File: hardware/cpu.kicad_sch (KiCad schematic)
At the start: 16 parts, among them J1 Conn_02x02_Odd_Even, U3 ESP32-C3-WROOM-02

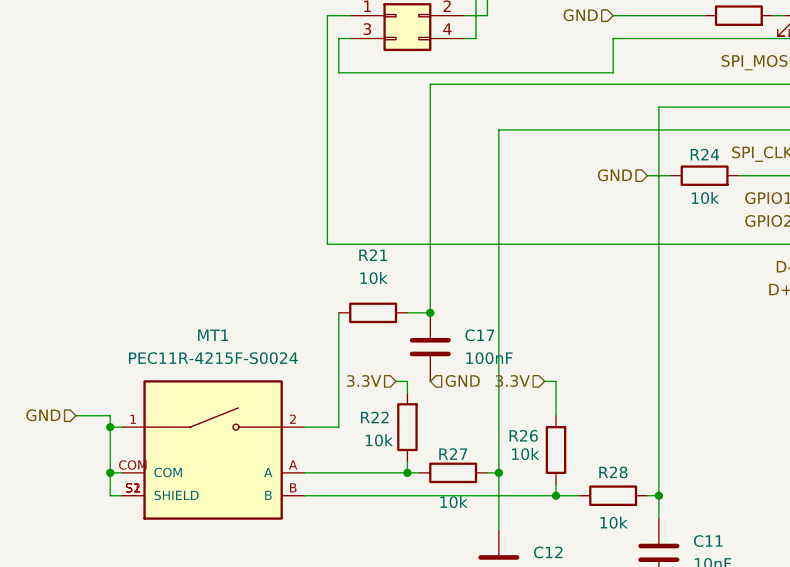
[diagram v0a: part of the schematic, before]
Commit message: Remove useless 10k resistor for PEC11 switch.
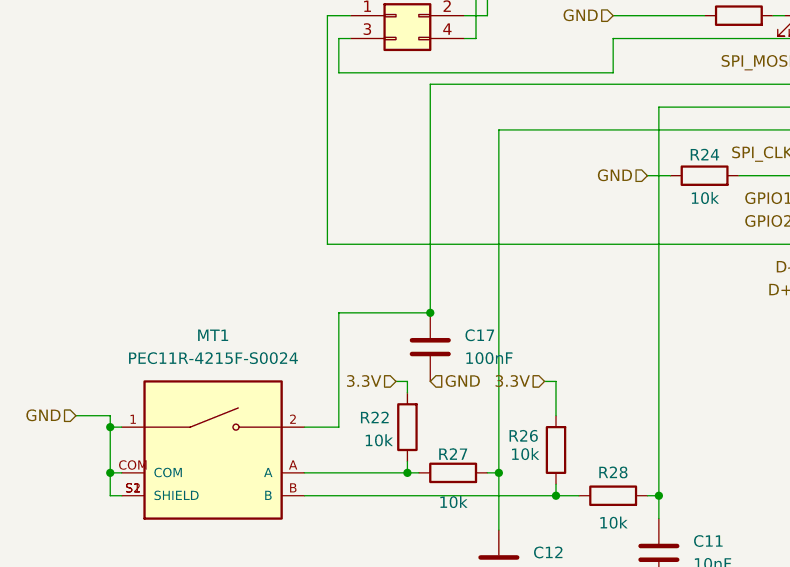
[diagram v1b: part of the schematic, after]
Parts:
- removed R21: 10k, Resistor_SMD:R_0805_2012Metric, symbol Device:R
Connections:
- net at MT1.2: now also C17.1, U3.15 (IO3)
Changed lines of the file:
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@@
+	(wire
+		(pts
+			(xy 62.23 93.98) (xy 72.39 93.98)
+		)
+		(stroke
+			(width 0)
+			(type default)
+		)
+	)
 	(wire
 		(pts
@@
 		(pts
 			(xy 78.74 27.94) (xy 78.74 60.96)
-		)
-		(stroke
-			(width 0)
-			(type default)
-		)
-	)
-	(wire
-		(pts
-			(xy 69.85 93.98) (xy 72.39 93.98)
 		)
 		(stroke
@@
 					(unit 1)
 				)
-			)
-		)
-	)
-	(symbol
-		(lib_id "Device:R")
-		(at 66.04 93.98 90)
-		(unit 1)
-		(exclude_from_sim no)
-		(in_bom yes)
-		(on_board yes)
-		(dnp no)
-		(fields_autoplaced yes)
-		(property "Reference" "R21"
-			(at 66.04 87.63 90)
-			(effects
-				(font
-					(size 1.27 1.27)
-				)
-			)
-		)
-		(property "Value" "10k"
-			(at 66.04 90.17 90)
-			(effects
-				(font
-					(size 1.27 1.27)
-				)
-			)
-		)
-		(property "Footprint" "Resistor_SMD:R_0805_2012Metric"
-			(at 66.04 95.758 90)
-			(effects
-				(font
-					(size 1.27 1.27)
-				)
-				(hide yes)
-			)
-		)
-		(property "Datasheet" "~"
-			(at 66.04 93.98 0)
-			(effects
-				(font
-					(size 1.27 1.27)
-				)
-				(hide yes)
-			)
-		)
-		(property "Description" "Resistor"
-			(at 66.04 93.98 0)
-			(effects
-				(font
-					(size 1.27 1.27)
-				)
-				(hide yes)
-			)
-		)
-		(pin "1"
-		)
-		(pin "2"
-		)
-		(instances
-			(project "nixie_clock"
-				(path "/90430e5f-7049-4de8-b92d-f897c4a89819/99bf9233-4f4b-4c20-a5a1-eeea9a6ff67a"
-					(reference "R21")
-					(unit 1)
-				)

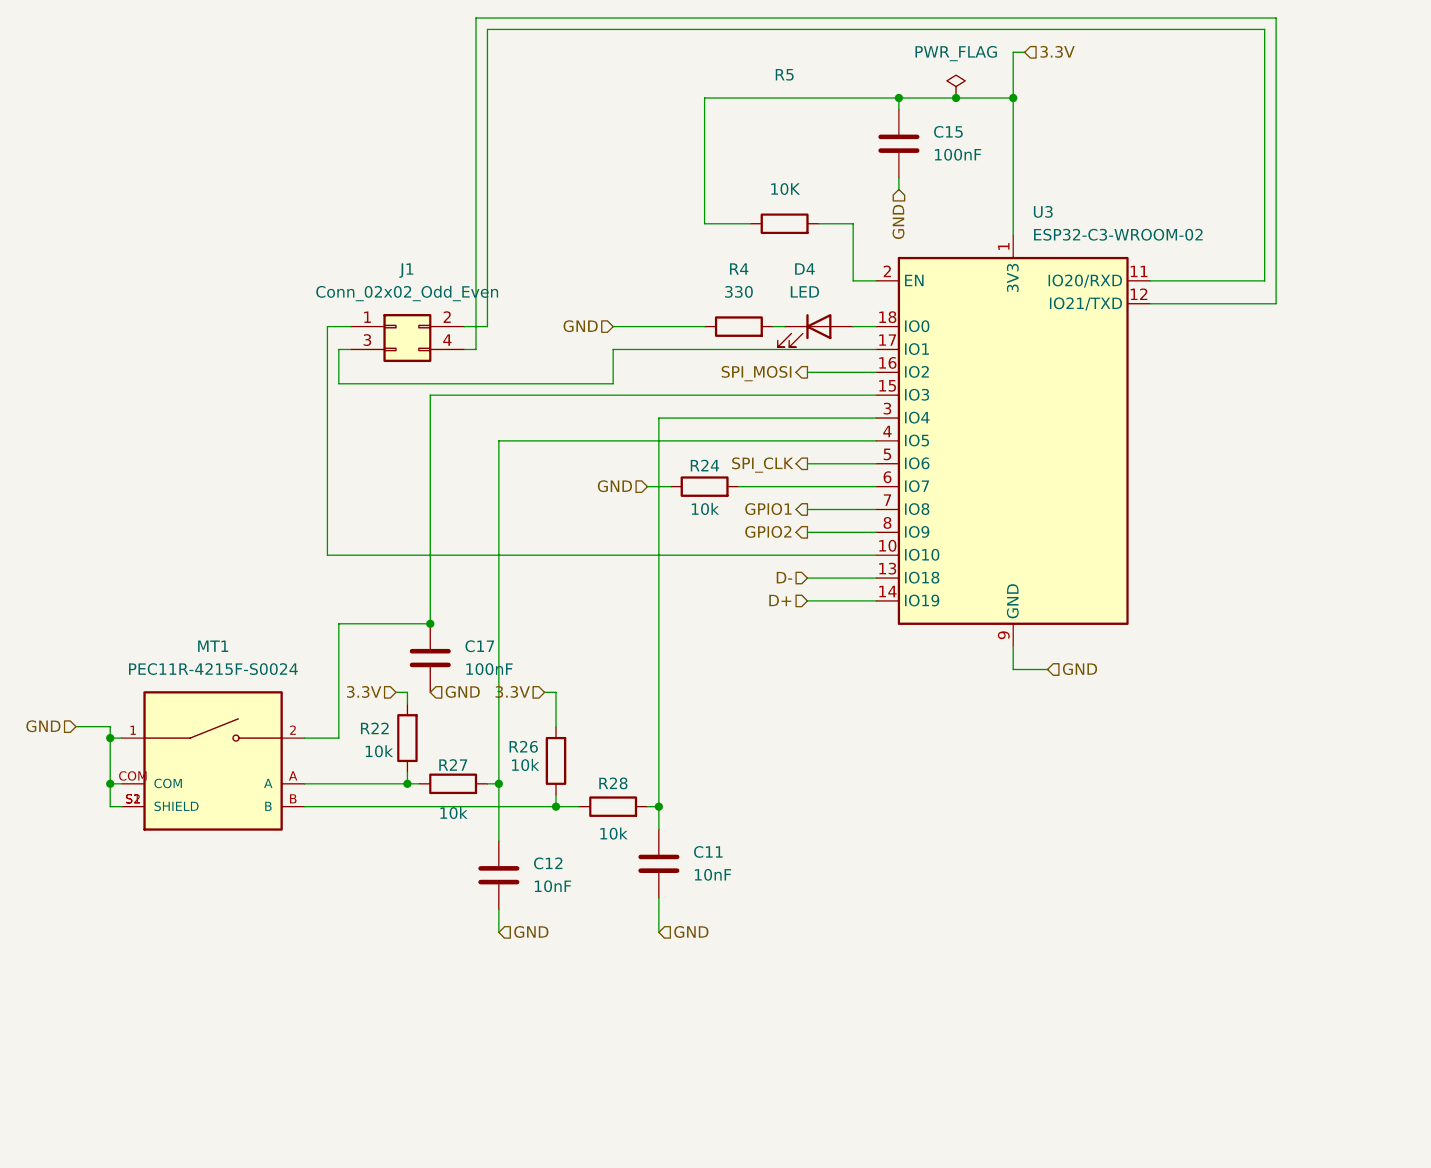
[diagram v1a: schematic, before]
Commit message: Add BOOT1 and RESET1 buttons. Add pullups on Boot strapping pins GPIO8,9. Fix EN, enable input.
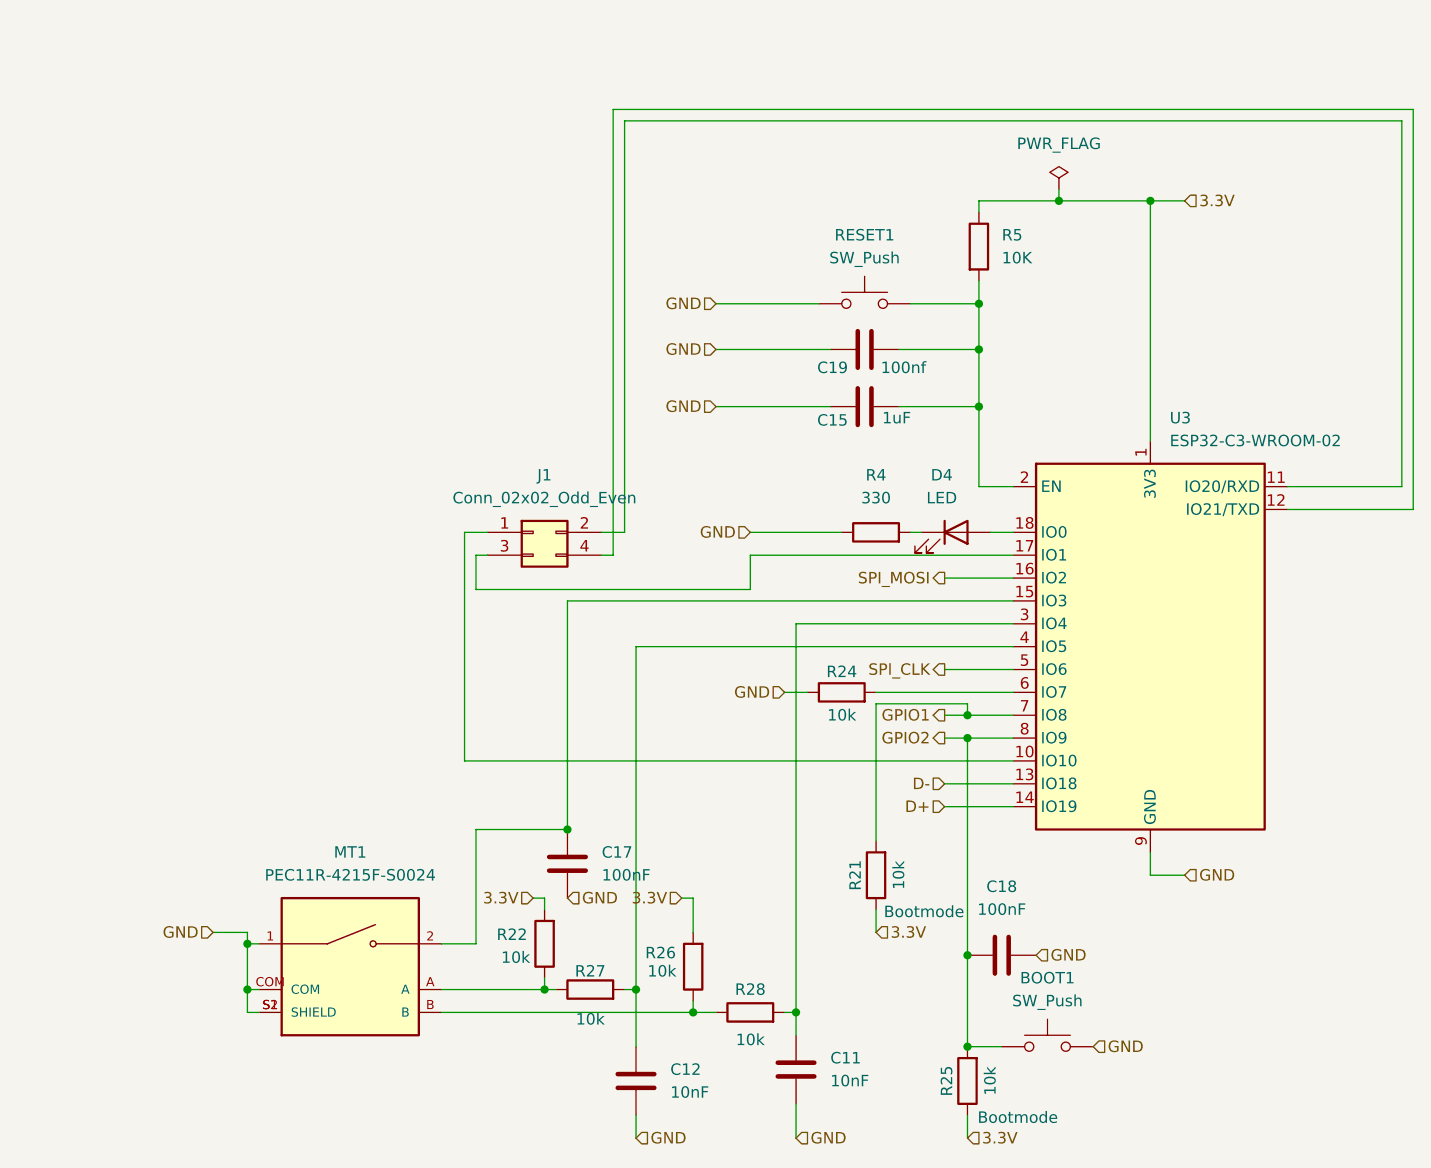
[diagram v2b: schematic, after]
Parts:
- added BOOT1, RESET1: SW_Push, Button_Switch_SMD:SW_SPST_Omron_B3FS-100xP, symbol Switch:SW_Push
- added C18: 100nF, Resistor_SMD:R_0805_2012Metric, symbol Device:C
- added C19: 100nf, Resistor_SMD:R_0805_2012Metric, symbol Device:C
- added R21, R25: 10k, Resistor_SMD:R_0805_2012Metric, symbol Device:R
- C15: value 100nF -> 1uF
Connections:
- net 3.3V: now also R21.1, R25.1; no longer C15.1
- net GND: now also C15.1, BOOT1.2, C18.2, C19.1, RESET1.1; no longer C15.2
- net GPIO1: now also R21.2
- net GPIO2: now also BOOT1.1, C18.1, R25.2
- net at R5.2, U3.2 (EN): now also C15.2, C19.2, RESET1.2
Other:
- moved on the sheet: C11, C12, C15, C17, D4, J1, MT1, R22, R24, R26, R27, R28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

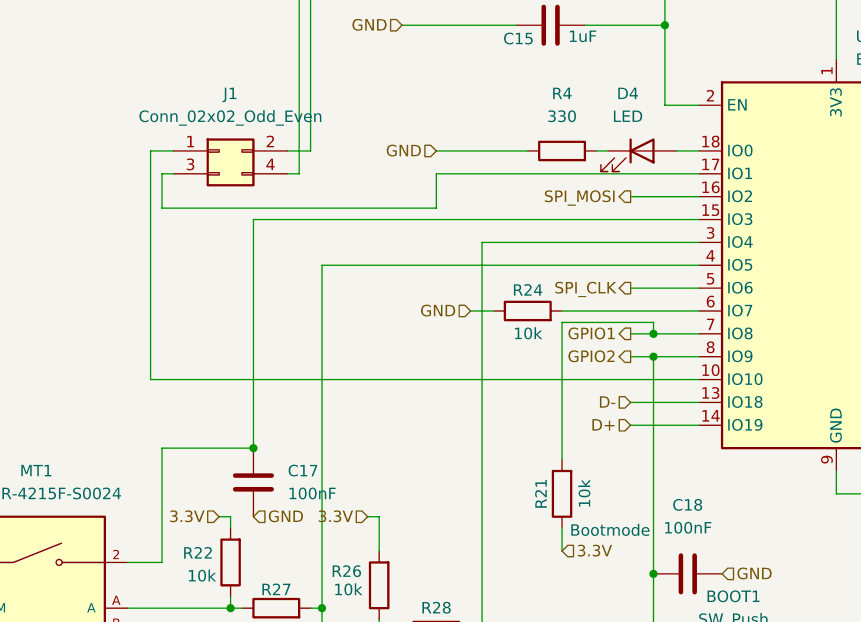
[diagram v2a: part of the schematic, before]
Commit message: Remap /LE and /BL to GPIO2 and GPIO1. SPI2 clk to GPIO6, SPI2 data to GPIO7.
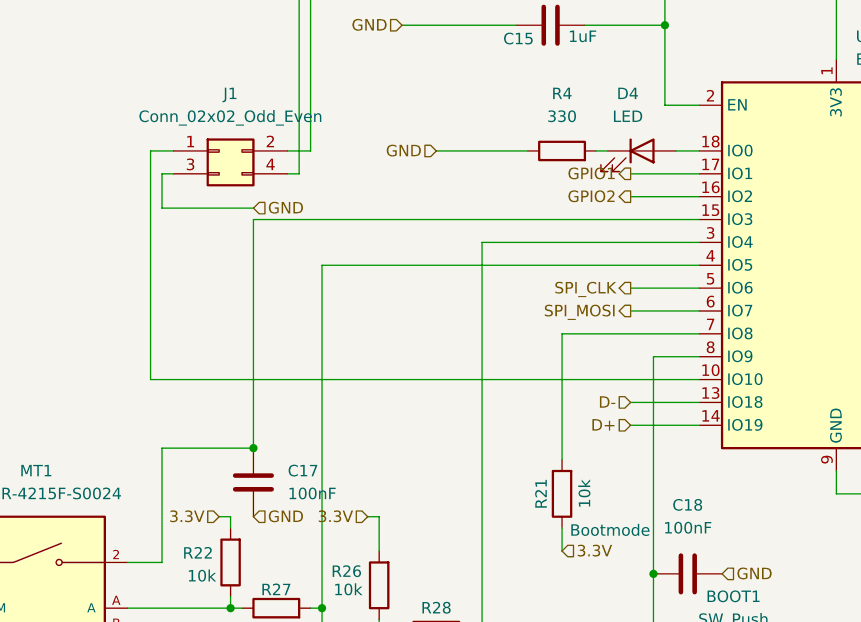
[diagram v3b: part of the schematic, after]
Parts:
- removed R24: 10k, Resistor_SMD:R_0805_2012Metric, symbol Device:R
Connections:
- net GND: now also J1.3 (Pin_3)
- net GPIO1: now also U3.17 (IO1); no longer R21.2, U3.7 (IO8)
- net GPIO2: now also U3.16 (IO2); no longer BOOT1.1, C18.1, R25.2, U3.8 (IO9)
- net SPI_MOSI: now also U3.6 (IO7); no longer U3.16 (IO2)
- new net: BOOT1.1, C18.1, R25.2, U3.8 (IO9)
- new net: R21.2, U3.7 (IO8)
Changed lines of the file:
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@@
-	)
-	(junction
-		(at 132.08 106.68)
-		(diameter 0)
-		(color 0 0 0 0)
 	)
 	(junction
@@
 	)
 	(junction
-		(at 132.08 104.14)
-		(diameter 0)
-		(color 0 0 0 0)
-	)
-	(junction
 		(at 133.35 58.42)
 		(diameter 0)
@@
 	(wire
 		(pts
-			(xy 129.54 104.14) (xy 132.08 104.14)
-		)
-		(stroke
-			(width 0)
-			(type default)
-		)
-	)
-	(wire
-		(pts
 			(xy 77.47 129.54) (xy 77.47 116.84)
 		)
@@
 	(wire
 		(pts
-			(xy 111.76 101.6) (xy 114.3 101.6)
-		)
-		(stroke
-			(width 0)
-			(type default)
-		)
-	)
-	(wire
-		(pts
 			(xy 132.08 106.68) (xy 132.08 130.81)
 		)
@@
 	(wire
 		(pts
-			(xy 132.08 102.87) (xy 121.92 102.87)
+			(xy 121.92 104.14) (xy 137.16 104.14)
 		)
 		(stroke
@@
 	(wire
 		(pts
-			(xy 132.08 104.14) (xy 132.08 102.87)
-		)
-		(stroke
-			(width 0)
-			(type default)
-		)
-	)
-	(wire
-		(pts
 			(xy 76.2 109.22) (xy 76.2 83.82)
 		)
@@
 	(wire
 		(pts
-			(xy 107.95 90.17) (xy 77.47 90.17)
+			(xy 129.54 86.36) (xy 137.16 86.36)
 		)
 		(stroke
@@
 	(wire
 		(pts
+			(xy 129.54 88.9) (xy 137.16 88.9)
+		)
+		(stroke
+			(width 0)
+			(type default)
+		)
+	)
+	(wire
+		(pts
 			(xy 104.14 63.5) (xy 116.84 63.5)
 		)
@@
 	(wire
 		(pts
-			(xy 107.95 86.36) (xy 107.95 90.17)
-		)
-		(stroke
-			(width 0)
-			(type default)
-		)
-	)
-	(wire
-		(pts
-			(xy 129.54 88.9) (xy 137.16 88.9)
-		)
-		(stroke
-			(width 0)
-			(type default)
-		)
-	)
-	(wire
-		(pts
 			(xy 113.03 137.16) (xy 111.76 137.16)
 		)
@@
 	(wire
 		(pts
-			(xy 121.92 102.87) (xy 121.92 118.11)
+			(xy 121.92 104.14) (xy 121.92 118.11)
 		)
 		(stroke
@@
 	(wire
 		(pts
+			(xy 129.54 101.6) (xy 137.16 101.6)
+		)
+		(stroke
+			(width 0)
+			(type default)
+		)
+	)
+	(wire
+		(pts
 			(xy 92.71 36.83) (xy 181.61 36.83)
 		)
@@
 	(wire
 		(pts
+			(xy 77.47 90.17) (xy 87.63 90.17)
+		)
+		(stroke
+			(width 0)
+			(type default)
+		)
+	)
+	(wire
+		(pts
 			(xy 133.35 78.74) (xy 137.16 78.74)
 		)
@@
 	(wire
 		(pts
-			(xy 132.08 104.14) (xy 137.16 104.14)
-		)
-		(stroke
-			(width 0)
-			(type default)
-		)
-	)
-	(wire
-		(pts
 			(xy 133.35 63.5) (xy 133.35 69.85)
 		)
@@
 	(wire
 		(pts
-			(xy 129.54 106.68) (xy 132.08 106.68)
-		)
-		(stroke
-			(width 0)
-			(type default)
-		)
-	)
-	(wire
-		(pts
 			(xy 95.25 134.62) (xy 95.25 140.97)
 		)
@@
 	(wire
 		(pts
-			(xy 107.95 86.36) (xy 137.16 86.36)
-		)
-		(stroke
-			(width 0)
-			(type default)
-		)
-	)
-	(wire
-		(pts
 			(xy 133.35 69.85) (xy 133.35 78.74)
 		)
@@
 	(wire
 		(pts
-			(xy 121.92 101.6) (xy 137.16 101.6)
-		)
-		(stroke
-			(width 0)
-			(type default)
-		)
-	)
-	(wire
-		(pts
 			(xy 83.82 124.46) (xy 85.09 124.46)
 		)
@@
 			(width 0)
 			(type default)
-		)
-	)
-	(hierarchical_label "GPIO1"
-		(shape output)
-		(at 129.54 104.14 180)
-		(effects
-			(font
-				(size 1.27 1.27)
-			)
-			(justify right)
 		)
 	)
@@
 		)
 	)
+	(hierarchical_label "GPIO1"
+		(shape output)
+		(at 129.54 86.36 180)
+		(effects
+			(font
+				(size 1.27 1.27)
+			)
+			(justify right)
+		)
+	)
 	(hierarchical_label "GND"
 		(shape input)
@@
 	(hierarchical_label "SPI_MOSI"
 		(shape output)
-		(at 129.54 88.9 180)
+		(at 129.54 101.6 180)
 		(effects
 			(font
@@
 	(hierarchical_label "GPIO2"
 		(shape output)
-		(at 129.54 106.68 180)
+		(at 129.54 88.9 180)
 		(effects
 			(font
@@
 	(hierarchical_label "GND"
 		(shape input)
-		(at 111.76 101.6 180)
-		(effects
-			(font
-				(size 1.27 1.27)
-			)
-			(justify right)
+		(at 87.63 90.17 0)
+		(effects
+			(font
+				(size 1.27 1.27)
+			)
+			(justify left)
 		)
 	)
@@
 					(unit 1)
 				)
-			)
-		)
-	)
-	(symbol
-		(lib_id "Device:R")
-		(at 118.11 101.6 90)
-		(unit 1)
-		(exclude_from_sim no)
-		(in_bom yes)
-		(on_board yes)
-		(dnp no)
-		(property "Reference" "R24"
-			(at 118.11 99.314 90)
-			(effects
-				(font
-					(size 1.27 1.27)
-				)
-			)
-		)
-		(property "Value" "10k"
-			(at 118.11 104.14 90)
-			(effects
-				(font
-					(size 1.27 1.27)
-				)
-			)
-		)
-		(property "Footprint" "Resistor_SMD:R_0805_2012Metric"
-			(at 118.11 103.378 90)
-			(effects
-				(font
-					(size 1.27 1.27)
-				)
-				(hide yes)
-			)
-		)
-		(property "Datasheet" "~"
-			(at 118.11 101.6 0)
-			(effects
-				(font
-					(size 1.27 1.27)
-				)
-				(hide yes)
-			)
-		)
-		(property "Description" "Resistor"
-			(at 118.11 101.6 0)
-			(effects
-				(font
-					(size 1.27 1.27)
-				)
-				(hide yes)
-			)
-		)
-		(pin "1"
-		)
-		(pin "2"
-		)
-		(instances
-			(project "nixie_clock"
-				(path "/90430e5f-7049-4de8-b92d-f897c4a89819/99bf9233-4f4b-4c20-a5a1-eeea9a6ff67a"
-					(reference "R24")
-					(unit 1)
-				)
